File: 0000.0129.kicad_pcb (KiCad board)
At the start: 2 copper layers, 90 x 70 mm, 101 parts, among them J1 BH254_LATCH, J3 Conn_01x11, Q2 20N06, Q5 20N06, T1 T80, U1 LT8304, U3 UCC21736, U4 UCC21736

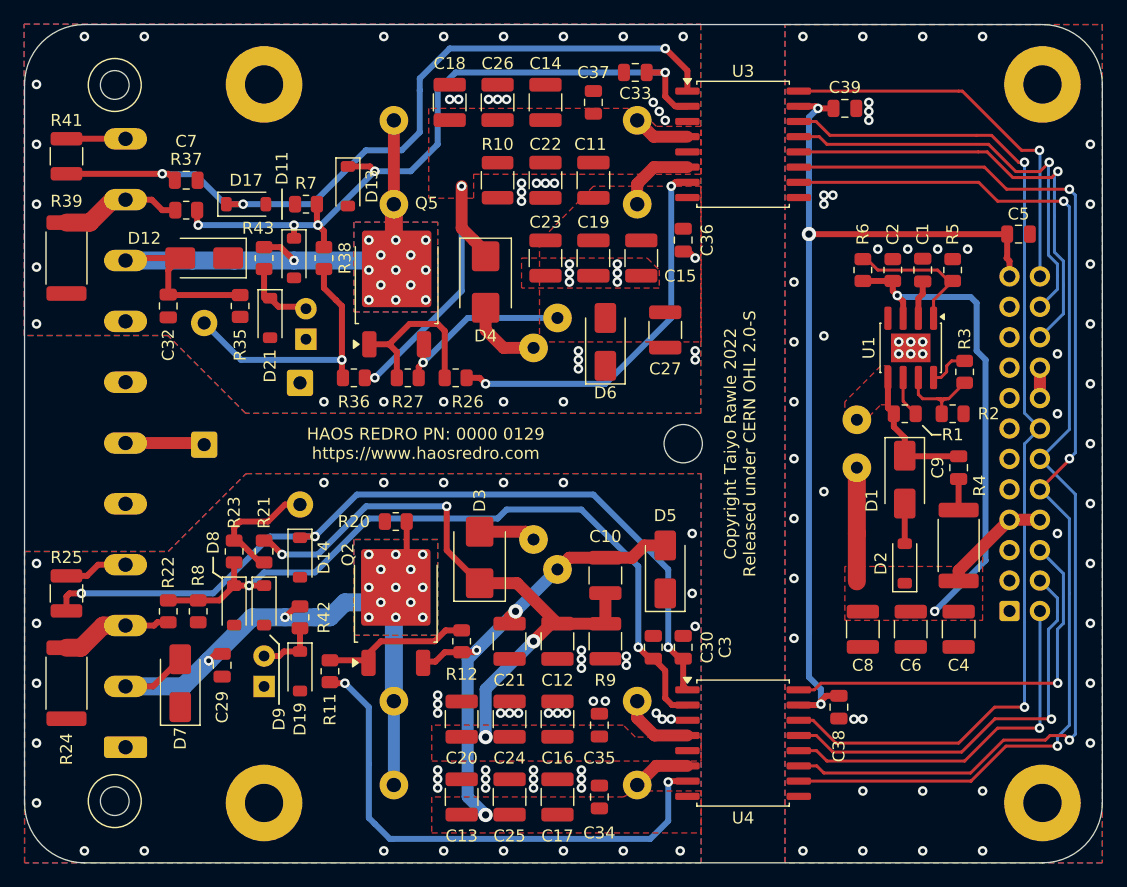
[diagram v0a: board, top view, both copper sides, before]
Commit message: PCB updated - screw hole clearances were incorrect.
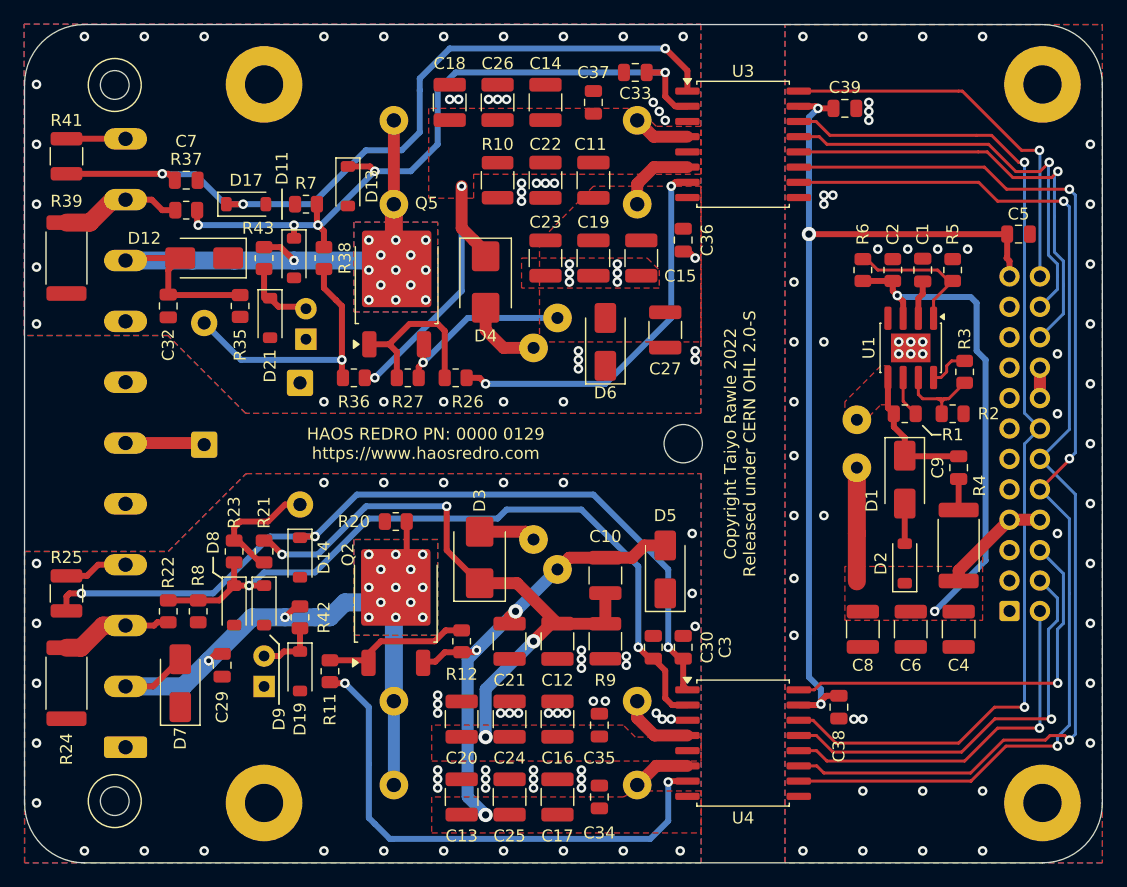
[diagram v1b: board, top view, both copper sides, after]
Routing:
- net GND2: vias 44 -> 46
- net GND1: vias 52 -> 54
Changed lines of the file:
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@@
 			(layers "*.Cu" "*.Mask")
 			(remove_unused_layers no)
+			(clearance 0.5)
 			(zone_connect 2)
 		)
@@
 			(layers "*.Cu" "*.Mask")
 			(remove_unused_layers no)
+			(clearance 0.5)
 			(zone_connect 2)
 		)
@@
 			(layers "*.Cu" "*.Mask")
 			(remove_unused_layers no)
+			(clearance 0.5)
 			(zone_connect 2)
 		)
@@
 			(layers "*.Cu" "*.Mask")
 			(remove_unused_layers no)
+			(clearance 0.5)
 			(zone_connect 2)
 		)
@@
 			(drill 3.2)
 			(layers "*.Cu" "*.Mask")
+			(clearance 5)
 		)
 		(pad "1" thru_hole circle
@@
 			(drill 2.4)
 			(layers "*.Cu" "*.Mask")
+			(clearance 0.5)
 		)
 		(pad "" np_thru_hole circle
@@
 			(drill 2.4)
 			(layers "*.Cu" "*.Mask")
+			(clearance 0.5)
 		)
 		(pad "1" thru_hole roundrect
@@
 	)
 	(via
-		(at 166.75 99)
+		(at 166.75 101)
 		(size 0.8)
 		(drill 0.4)
@@
 	)
 	(via
-		(at 164.25 96.25)
+		(at 164.25 96)
 		(size 0.8)
 		(drill 0.4)
@@
 	)
 	(via
-		(at 164.25 101.25)
+		(at 164.25 101)
 		(size 0.8)
 		(drill 0.4)
@@
 	)
 	(via
-		(at 164.25 111.25)
+		(at 164.25 111)
 		(size 0.8)
 		(drill 0.4)
@@
 	)
 	(via
-		(at 166.75 86)
+		(at 166.75 86.5)
 		(size 0.8)
 		(drill 0.4)
@@
 	)
 	(via
+		(at 125 129)
+		(size 0.8)
+		(drill 0.4)
+		(layers "F.Cu" "B.Cu")
+		(free yes)
+		(net 8)
+	)
+	(via
 		(at 140 129)
 		(size 0.8)
@@
 	)
 	(via
+		(at 115 129)
+		(size 0.8)
+		(drill 0.4)
+		(layers "F.Cu" "B.Cu")
+		(free yes)
+		(net 8)
+	)
+	(via
 		(at 145.25 117.5)
 		(size 0.8)
@@
 	)
 	(via
+		(at 125 61)
+		(size 0.8)
+		(drill 0.4)
+		(layers "F.Cu" "B.Cu")
+		(free yes)
+		(net 9)
+	)
+	(via
 		(at 152.5 66.5)
 		(size 0.8)
@@
 	)
 	(via
+		(at 115 61)
+		(size 0.8)
+		(drill 0.4)
+		(layers "F.Cu" "B.Cu")
+		(free yes)
+		(net 9)
+	)
+	(via
 		(at 138.75 66.25)
 		(size 0.8)
@@
 			(thermal_gap 0.508)
 			(thermal_bridge_width 0.508)
+			(smoothing fillet)
+			(radius 1)
 		)
 		(polygon
@@
 			(thermal_bridge_width 0.508)
 			(smoothing fillet)
-			(radius 0.5)
+			(radius 1)
 		)
 		(polygon
@@
 			(thermal_gap 0.508)
 			(thermal_bridge_width 0.508)
+			(smoothing fillet)
+			(radius 1)
 		)
 		(polygon
